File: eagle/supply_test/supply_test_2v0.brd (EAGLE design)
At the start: 25.4 x 25.4 mm, 29 parts, among them J21 AC_INFILM, Q1 2N7002, U1 TPS62122

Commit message: placement done
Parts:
- added TP5: TP_STD, skyspecs:TP
- moved R11 64.1 mm to (10.3, 0.32), turned to 180 degrees
- moved TP4 54.6 mm to (8.89, -14.0)
- moved TP3 51.2 mm to (6.35, -14.0)
- moved TP2 49.0 mm to (-5.08, -14.0)
- moved TP1 45.5 mm to (-7.62, -14.0)
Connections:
- net PS_!EN!: now also TP5.P$1
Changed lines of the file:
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@@
 <attribute name="DIGIKEY_2" value="AE9888-ND" x="25.4" y="-16.51" size="1.778" layer="27" display="off"/>
 </element>
-<element name="TP1" library="skyspecs" package="TP" value="TP_STD" x="-25.4" y="27.94">
-<attribute name="DIGIKEY" value="5000K-ND " x="0" y="0" size="1.778" layer="27" display="off"/>
+<element name="TP1" library="skyspecs" package="TP" value="TP_STD" x="-7.62" y="-13.97">
+<attribute name="DIGIKEY" value="5000K-ND " x="17.78" y="-41.91" size="1.778" layer="27" display="off"/>
 </element>
-<element name="TP2" library="skyspecs" package="TP" value="TP_STD" x="-30.48" y="27.94">
-<attribute name="DIGIKEY" value="5001K-ND" x="0" y="0" size="1.778" layer="27" display="off"/>
+<element name="TP2" library="skyspecs" package="TP" value="TP_STD" x="-5.08" y="-13.97">
+<attribute name="DIGIKEY" value="5001K-ND" x="25.4" y="-41.91" size="1.778" layer="27" display="off"/>
 </element>
 <element name="D3" library="powerfilm" package="TO-253-4" value="BRIDGE_BGX" x="-3.01625" y="-0.9525">
@@
 <attribute name="DIGIKEY" value="2N7002WCT-ND" x="-20.6375" y="46.6725" size="1.778" layer="27" rot="R180" display="off"/>
 </element>
-<element name="R11" library="rcl" package="R0603" value="4.99k" x="-43.18" y="35.56"/>
+<element name="R11" library="rcl" package="R0603" value="4.99k" x="10.31875" y="0.3175" rot="R180"/>
 <element name="C7" library="rcl" package="C0402" value="4.7uF" x="4.92125" y="5.1562" rot="R270"/>
 <element name="C8" library="rcl" package="C0402" value="0.1uF" x="6.19125" y="5.1562" rot="R270"/>
@@
 <element name="R5" library="rcl" package="R0603" value="NP" x="0.15875" y="-0.635"/>
 <element name="R6" library="rcl" package="R0603" value="NP" x="0.15875" y="-1.905" rot="R180"/>
-<element name="TP3" library="skyspecs" package="TP" value="TP_STD" x="-44.45" y="-20.32">
-<attribute name="DIGIKEY" value="5000K-ND " x="-44.45" y="-20.32" size="1.778" layer="27" display="off"/>
+<element name="TP3" library="skyspecs" package="TP" value="TP_STD" x="6.35" y="-13.97">
+<attribute name="DIGIKEY" value="5000K-ND " x="6.35" y="-13.97" size="1.778" layer="27" display="off"/>
 </element>
-<element name="TP4" library="skyspecs" package="TP" value="TP_STD" x="-44.45" y="-25.4"/>
+<element name="TP4" library="skyspecs" package="TP" value="TP_STD" x="8.89" y="-13.97"/>
+<element name="TP5" library="skyspecs" package="TP" value="TP_STD" x="11.43" y="-13.97"/>
 </elements>
 <signals>
@@
 <contactref element="R8" pad="1"/>
 <contactref element="TP3" pad="P$1"/>
-<wire x1="-7.14375" y1="7.67625" x2="-44.45" y2="-20.32" width="0" layer="19" extent="1-1"/>
+<wire x1="-7.14375" y1="7.67625" x2="6.35" y2="-13.97" width="0" layer="19" extent="1-1"/>
 <wire x1="-5.55625" y1="7.67625" x2="-7.14375" y2="7.67625" width="0" layer="19" extent="1-1"/>
 <wire x1="-1.8796" y1="8.0618" x2="-5.55625" y2="7.67625" width="0" layer="19" extent="1-1"/>
@@
 <wire x1="3.7338" y1="3.595" x2="4.92125" y2="4.5062" width="0" layer="19" extent="1-1"/>
 <wire x1="2.76375" y1="3.81" x2="3.7338" y2="3.595" width="0" layer="19" extent="1-1"/>
-<wire x1="-30.48" y1="27.94" x2="-2.01625" y2="0.0475" width="0" layer="19" extent="1-1"/>
-<wire x1="-42.33" y1="35.56" x2="-30.48" y2="27.94" width="0" layer="19" extent="1-1"/>
+<wire x1="-5.08" y1="-13.97" x2="-2.01625" y2="0.0475" width="0" layer="19" extent="1-1"/>
 </signal>
 <signal name="VCC">
@@
 <wire x1="3.65125" y1="2.27875" x2="3.7338" y2="5.295" width="0" layer="19" extent="1-1"/>
 <wire x1="1.00875" y1="-0.635" x2="3.65125" y2="2.27875" width="0" layer="19" extent="1-1"/>
-<wire x1="-25.4" y1="27.94" x2="2.76375" y2="5.3975" width="0" layer="19" extent="1-1"/>
+<wire x1="-7.62" y1="-13.97" x2="2.76375" y2="5.3975" width="0" layer="19" extent="1-1"/>
 </signal>
 <signal name="N$4">
@@
 <contactref element="R11" pad="1"/>
 <contactref element="Q1" pad="P1"/>
-<wire x1="-44.03" y1="35.56" x2="10.9425" y2="1.5725" width="0" layer="19" extent="1-1"/>
+<contactref element="TP5" pad="P$1"/>
+<wire x1="11.16875" y1="0.3175" x2="11.43" y2="-13.97" width="0" layer="19" extent="1-1"/>
+<wire x1="10.9425" y1="1.5725" x2="11.16875" y2="0.3175" width="0" layer="19" extent="1-1"/>
 </signal>
 <signal name="N$9">
@@
 <contactref element="C9" pad="1"/>
 <contactref element="TP4" pad="P$1"/>
-<wire x1="1.74625" y1="8.343" x2="-44.45" y2="-25.4" width="0" layer="19" extent="1-1"/>
+<wire x1="1.74625" y1="8.343" x2="8.89" y2="-13.97" width="0" layer="19" extent="1-1"/>
 <wire x1="3.65125" y1="8.47" x2="1.74625" y2="8.343" width="0" layer="19" extent="1-1"/>
 <wire x1="9.89875" y1="8.4582" x2="3.65125" y2="8.47" width="0" layer="19" extent="1-1"/>

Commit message: routing
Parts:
- moved R2 1.96 mm to (0.16, 1.11), turned to 0 degrees
- moved C4 0.49 mm to (2.22, 7.59)
- moved R7 0.16 mm to (3.49, 7.62)
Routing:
- net N$4: track 0.00 -> 10.0 mm
- net VCC: track 0.00 -> 8.77 mm
- net N$2: track 0.00 -> 7.38 mm, vias 0 -> 1
- net N$1: track 0.00 -> 5.47 mm
- net N$7: track 0.00 -> 4.07 mm
- net N$16: track 0.00 -> 1.91 mm, vias 1 -> 2
- net N$8: track 0.00 -> 1.34 mm
- net GND: track 0.00 -> 1.27 mm
- net N$5: track 0.00 -> 1.23 mm
- added copper zone on layer 1, net +3V3
- added copper zone on layer 1, net N$13
- added copper zone on layer 1, net N$3
- added copper zone on layer 1, net VCC

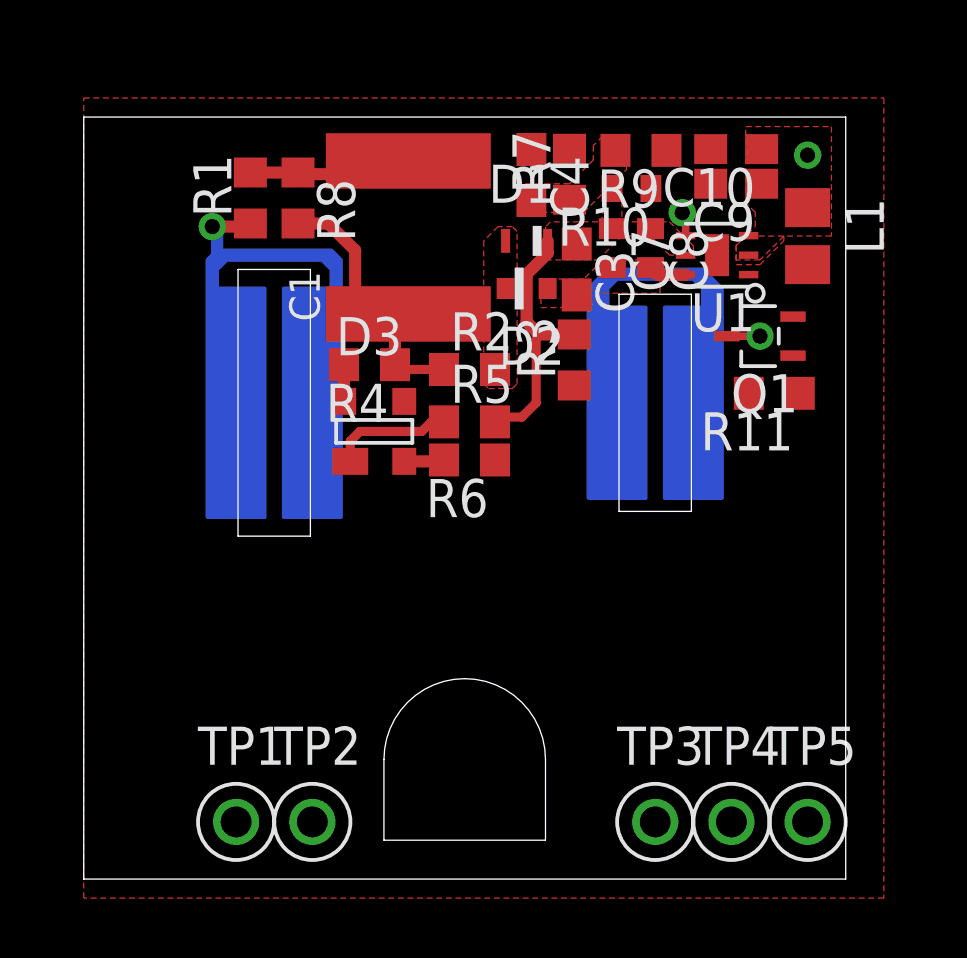
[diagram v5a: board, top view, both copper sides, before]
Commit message: added pot to supply test
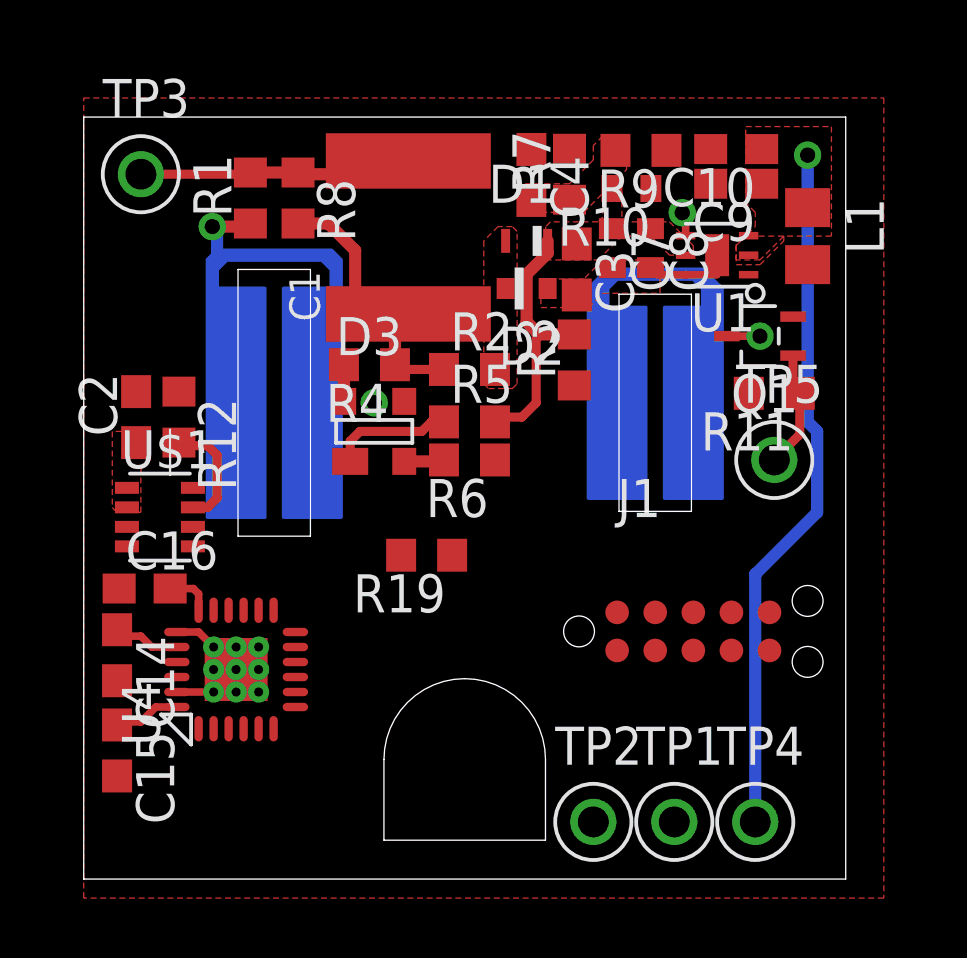
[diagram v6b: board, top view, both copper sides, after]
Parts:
- added C14, C2: 0.1uF, rcl:C0603
- added C15: 10uF, rcl:C0603
- added C16: 470nF, rcl:C0603
- added J1: JTAG_14PIN_IDC-NL, ibat:TC2050-IDC-NL-430
- added R12: 660, rcl:R0603
- added R19: 47k, rcl:R0603
- added U$1: AD524, powerfilm:SOT-23-8
- added U4: MSP430FR5738, powerfilm:VQFN-24
- R11: value 4.99k -> 47k
- moved TP3 27.6 mm to (-10.8, 7.62)
- moved TP1 14.6 mm to (6.99, -14.0)
- moved TP5 12.1 mm to (10.3, -1.91)
- moved TP2 9.37 mm to (4.29, -14.0)
- moved TP4 0.79 mm to (9.68, -14.0)
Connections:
- new net N$12: R12.2, U$1.P7
- new net N$23: C16.2, U4.P18
- new net RST: J1.P10, R19.1, U4.P12
- new net SCL: U$1.P4, U4.P17
- new net SDA: U$1.P5, U4.P16
- new net TCK: J1.P7, U4.P10
- new net TDI: J1.P3, U4.P8
- new net TDO: J1.P1, U4.P7
- new net TEST: J1.P8, U4.P11
- new net TMS: J1.P5, U4.P9
- net +3V3: now also C14.1, C15.1, C2.1, J1.P2, R19.2, U$1.P1, U$1.P2, U4.P20, U4.P24
- net GND: now also C14.2, C15.2, C16.1, C2.2, J1.P9, R12.1, U$1.P3, U$1.P6, U4.G1, U4.G2, U4.G3, U4.G4, U4.G5, U4.G6, U4.G7, U4.G8, U4.G9, U4.P19, U4.P23, U4.PAD
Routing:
- net +3V3: track 0.00 -> 27.7 mm
- net GND: track 1.27 -> 8.62 mm
- net PS_!EN!: track 0.00 -> 3.92 mm
- net N$12: track 0.00 -> 3.81 mm
- net N$1: track 5.47 -> 9.14 mm
- net N$23: track 0.00 -> 1.57 mm

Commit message: finished routing in new features
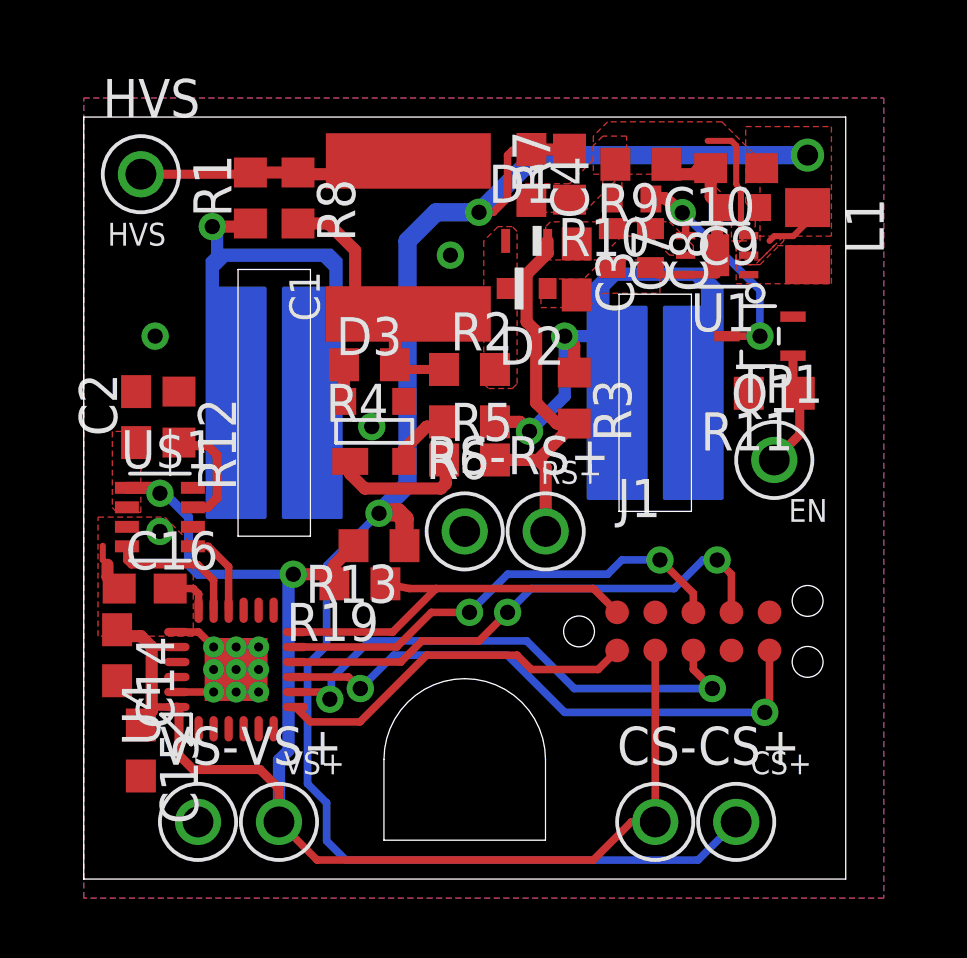
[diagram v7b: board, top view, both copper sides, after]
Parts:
- removed TP2, TP4, TP5: TP_STD, skyspecs:TP
- added CS+, CS-, RS+, RS-, VS+, VS-: TP_STD, skyspecs:TP
- added R13: 10, rcl:R0603
- C9: device rcl:C0603 -> rcl:C0402
- moved TP1 12.5 mm to (10.3, -1.91)
- moved R19 2.42 mm to (-3.49, -6.03)
- moved R3 1.27 mm to (3.65, 0.16), turned to 270 degrees
- moved R5 1.27 mm to (0.16, -1.91)
- moved R6 1.27 mm to (0.16, -0.64)
- moved C9 0.81 mm to (9.21, 6.51)
- moved C15 0.79 mm to (-10.8, -11.6)
- moved C10 0.63 mm to (9.05, 7.82)
- moved R9 0.46 mm to (5.87, 7.95)
- moved R10 0.35 mm to (5.56, 6.79)
- renumbered TP3 to HVS
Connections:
- new net N$11: C10.1, C4.1, C9.1, CS+.P$1, L1.1, R13.1, R7.2, U1.P2
- net +3V3: now also CS-.P$1, R13.2, VS+.P$1; no longer C10.1, C4.1, C9.1, L1.1, R7.2, TP4.P$1, U1.P2
- net GND: now also RS-.P$1, VS-.P$1; no longer TP2.P$1
- net PS_!EN!: now also TP1.P$1; no longer TP5.P$1
- net VCC: now also RS+.P$1; no longer TP1.P$1
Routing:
- net N$11: track 0.00 -> 59.2 mm, vias 0 -> 3
- net +3V3: track 27.7 -> 51.5 mm, vias 1 -> 2
- net TMS: track 0.00 -> 19.2 mm, vias 0 -> 2
- net TCK: track 0.00 -> 17.4 mm, vias 0 -> 2
- net TDI: track 0.00 -> 17.4 mm, vias 0 -> 2
- net N$6: track 0.00 -> 16.9 mm, vias 0 -> 2
- net TEST: track 0.00 -> 15.6 mm, vias 0 -> 2
- net RST: track 0.00 -> 13.4 mm
- net TDO: track 0.00 -> 12.3 mm
- net GND: track 8.62 -> 15.5 mm, vias 0 -> 4
- net N$16: track 1.91 -> 8.33 mm
- net SCL: track 0.00 -> 4.63 mm
- net VCC: track 8.77 -> 13.0 mm
- net N$13: track 0.00 -> 4.16 mm
- net SDA: track 0.00 -> 2.92 mm
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- added copper zone on layer 16, net GND
- added copper zone on layer 1, net N$11
- added copper zone on layer 1, net N$9
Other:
- board text added: "CS+"
- board text added: "EN"
- board text added: "HVS"
- board text added: "RS+"
- board text added: "VS+"

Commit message: all parts numbered in supply test v2
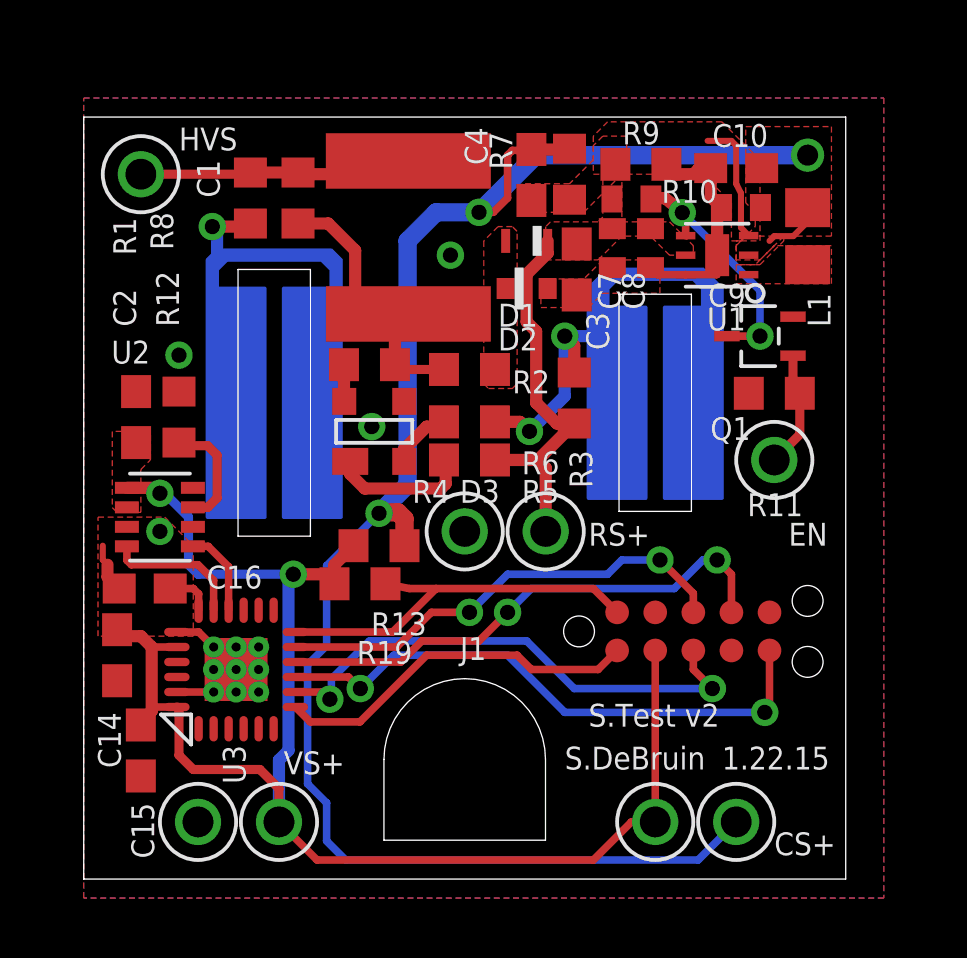
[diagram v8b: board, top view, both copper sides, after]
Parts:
- C3: value (none) -> 33uF
- R10: value 4.99k -> 10k
- renumbered U$1 to U2, U4 to U3
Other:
- board text added: "1.22.15"
- board text added: "S.DeBruin"
- board text added: "S.Test v2"
